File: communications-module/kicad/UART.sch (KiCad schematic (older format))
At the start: 20 parts, among them U11 FONA_3G, U12 TPS2064, U13 RockBLOCK, U14 SN74LV4052A, U15 TPS2064, U16 FGPMMOPA6H, U17 uFL_conn, U18 SN74LV4052A, U19 Gateway Module LORA

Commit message: Communications Module update
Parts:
- JP18, JP19, JP20, JP21: footprint (none) -> Socket_Strips:Socket_Strip_Straight_1x02_Pitch2.54mm
- JP22: renamed from JP?; footprint (none) -> Socket_Strips:Socket_Strip_Straight_1x02_Pitch2.54mm
- gave numbers to parts that had none: 1

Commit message: Communications Module update
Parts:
- U11: footprint FONA_3G:FONA_3G -> FONA_3G:FONA_3G_vertical
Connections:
- net FONA_3V3: no longer U20.7 (OUT1)
- net FONA_VBAT: now also U20.7 (OUT1)
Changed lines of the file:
@@
 U 1 1 589D996F
 P 1425 2045
-F 0 "U11" H 1325 3195 60  0000 C CNN
+F 0 "U11" H 1370 3190 60  0000 C CNN
 F 1 "FONA_3G" H 1475 3095 60  0000 C CNN
-F 2 "FONA_3G:FONA_3G" H 1500 1070 60  0001 C CNN
+F 2 "FONA_3G:FONA_3G_vertical" H 1500 1070 60  0001 C CNN
 F 3 "" H 1475 3170 60  0000 C CNN
 	1    1425 2045
@@
 U 1 1 589D9A2E
 P 3495 2160
-F 0 "U13" H 3520 3060 60  0000 C CNN
+F 0 "U13" H 3500 3055 60  0000 C CNN
 F 1 "RockBLOCK" H 3520 2960 60  0000 C CNN
 F 2 "" H 3545 3035 60  0000 C CNN
@@
 Wire Wire Line
 	2740 4605 2865 4605
-Text GLabel 2865 4415 2    60   Input ~ 0
-FONA_3V3
 Text GLabel 1760 4490 0    60   Input ~ 0
 ENABLE-FONA
@@
 Wire Wire Line
 	2740 4415 2865 4415
+Text GLabel 2865 4415 2    60   Input ~ 0
+FONA_VBAT
 $EndSCHEMATC

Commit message: All gerbers update
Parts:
- added R?: 10K, 0603_handsolder:0603_HandSoldering, symbol R
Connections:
- net ENABLE-ROCK: now also R?.2
- net FONA_CTS: now also U11.8 (RTS_IN); no longer U11.10 (CTS)
- net FONA_RTS: now also U11.10 (CTS); no longer U11.8 (RTS_IN)
- net FONA_RX: now also U11.7 (TX); no longer U11.6 (RX)
- net FONA_TX: now also U11.6 (RX); no longer U11.7 (TX)
- net ROCK_CTS: no longer U13.5 (CTS)
- net ROCK_RX: now also U13.3 (TXD); no longer U13.2 (RXD)
- net ROCK_TX: now also U13.2 (RXD); no longer U13.3 (TXD)
- net at U13.12 (ON_OFF): now also R?.1
- net FONA_DTR: no longer names the net of U11.9 (DTR)
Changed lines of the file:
@@
 	0    -1   -1   0
 $EndComp
+Text GLabel 1850 1745 2    60   Input ~ 0
+FONA_RX
 Text GLabel 1850 1645 2    60   Input ~ 0
-FONA_RX
-Text GLabel 1850 1745 2    60   Input ~ 0
 FONA_TX
 NoConn ~ 1850 2545
@@
 Text GLabel 4870 6220 0    60   Input ~ 0
 FONA_CTS
+Text GLabel 1850 2045 2    60   Input ~ 0
+FONA_RTS
 Text GLabel 1850 1845 2    60   Input ~ 0
-FONA_RTS
-Text GLabel 1850 2045 2    60   Input ~ 0
 FONA_CTS
 NoConn ~ 4870 5820
@@
 	1    0    0    -1
 $EndComp
+Text GLabel 3895 1585 2    60   Input ~ 0
+ROCK_TX
 Text GLabel 3895 1685 2    60   Input ~ 0
-ROCK_TX
-Text GLabel 3895 1585 2    60   Input ~ 0
 ROCK_RX
 Text GLabel 3895 1485 2    60   Input ~ 0
 ROCK_RTS
-Text GLabel 3895 1885 2    60   Input ~ 0
+Text GLabel 4540 1330 2    60   Input ~ 0
 ROCK_CTS
 $Comp
@@
 	0    -1   -1   0
 $EndComp
-Text GLabel 1850 1945 2    60   Input ~ 0
-FONA_DTR
 Text GLabel 3895 1785 2    60   Input ~ 0
 ROCK_5V
-NoConn ~ 3895 2585
 $Comp
 L +3.3V #PWR096
@@
 Text GLabel 2865 4415 2    60   Input ~ 0
 FONA_VBAT
+$Comp
+L R R?
+U 1 1 5894C116
+P 4045 2585
+F 0 "R?" V 4125 2585 50  0000 C CNN
+F 1 "10K" V 4045 2585 50  0000 C CNN
+F 2 "0603_handsolder:0603_HandSoldering" V 3975 2585 30  0001 C CNN
+F 3 "" H 4045 2585 30  0000 C CNN
+	1    4045 2585
+	0    -1   -1   0
+$EndComp
+Text GLabel 4195 2585 2    60   Input ~ 0
+ENABLE-ROCK
+NoConn ~ 1850 1945
 $EndSCHEMATC

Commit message: Communications Module schematic update
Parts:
- gave numbers to parts that had none: 1
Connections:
- net FONA_CTS: now also U14.14 (1Y1); no longer U14.5 (2Y1)
- net FONA_RTS: now also U14.5 (2Y1); no longer U14.14 (1Y1)
- net FONA_RX: now also U18.5 (2Y1); no longer U18.14 (1Y1)
- net FONA_TX: now also U18.14 (1Y1); no longer U18.5 (2Y1)
- net GPS_RX: now also U16.9 (TX), U18.1 (2Y0); no longer U16.10 (RX), U18.12 (1Y0)
- net GPS_TX: now also U16.10 (RX), U18.12 (1Y0); no longer U16.9 (TX), U18.1 (2Y0)
- net ROCK_CTS: now also U13.5 (CTS), U14.15 (1Y2); no longer U14.2 (2Y2)
- net ROCK_RTS: now also U14.2 (2Y2); no longer U14.15 (1Y2)
- net ROCK_RX: now also U13.2 (RXD), U18.2 (2Y2); no longer U13.3 (TXD), U18.15 (1Y2)
- net ROCK_TX: now also U13.3 (TXD), U18.15 (1Y2); no longer U13.2 (RXD), U18.2 (2Y2)
- net UART_A renamed UMUX_SEL0
- net UART_B renamed UMUX_SEL1
- net UART_INH renamed UMUX_INH
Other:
- moved on the sheet: JP18, JP19, JP22, U12, U14, U17, U20

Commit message: Communications Module update
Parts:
- U13: footprint (none) -> RockBlock:RockBlock_vertical
- U19: footprint RaspberryPi:RaspberryPi -> (none)
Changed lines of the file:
@@
 F 0 "U13" H 3500 3055 60  0000 C CNN
 F 1 "RockBLOCK" H 3520 2960 60  0000 C CNN
-F 2 "" H 3545 3035 60  0000 C CNN
+F 2 "RockBlock:RockBlock_vertical" H 3615 1315 60  0001 C CNN
 F 3 "" H 3545 3035 60  0000 C CNN
 	1    3495 2160
@@
 F 0 "U19" H 9445 3295 60  0000 C CNN
 F 1 "Gateway Module LORA" H 9450 3195 60  0000 C CNN
-F 2 "RaspberryPi:RaspberryPi" H 9405 1030 60  0001 C CNN
+F 2 "" H 9405 1030 60  0001 C CNN
 F 3 "" H 9405 2080 60  0000 C CNN
 	1    9405 2080

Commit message: Communications Module footprints update
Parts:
- U19: footprint (none) -> Solarcast_Gateway_Module:Solarcast_Gateway_Module
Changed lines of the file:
@@
 F 0 "U19" H 9445 3295 60  0000 C CNN
 F 1 "Gateway Module LORA" H 9450 3195 60  0000 C CNN
-F 2 "" H 9405 1030 60  0001 C CNN
+F 2 "Solarcast_Gateway_Module:Solarcast_Gateway_Module" H 9405 1030 60  0001 C CNN
 F 3 "" H 9405 2080 60  0000 C CNN
 	1    9405 2080

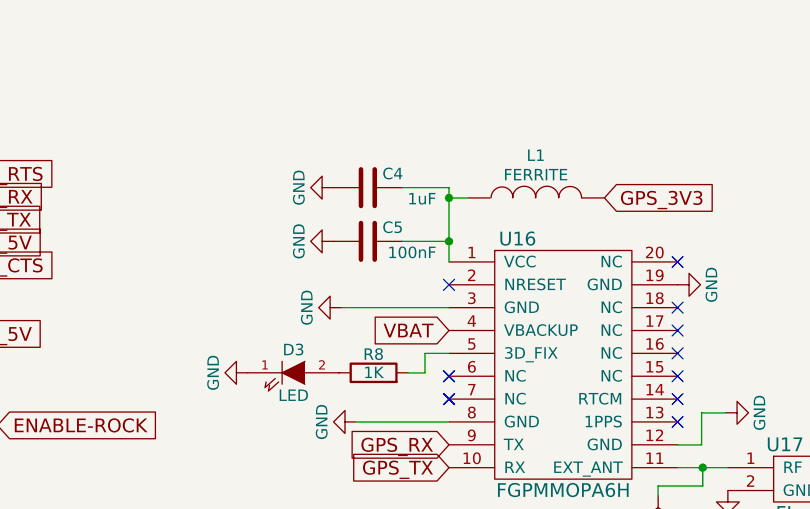
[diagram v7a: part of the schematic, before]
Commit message: Communications Module PCB components placed
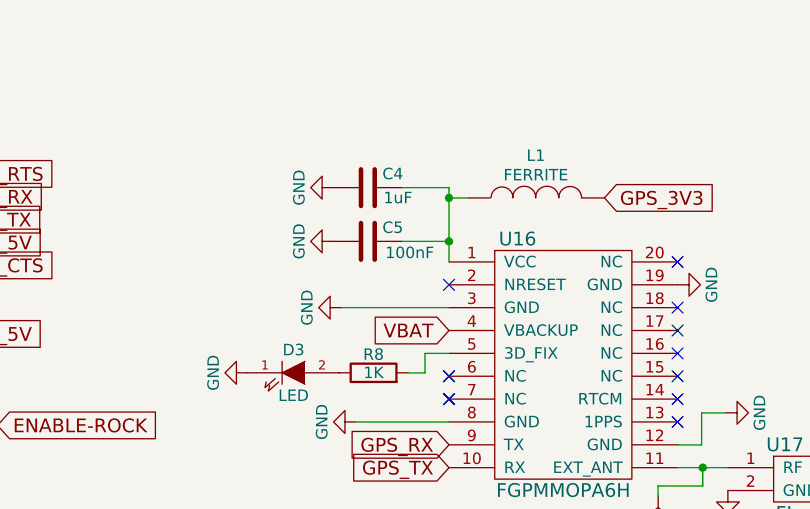
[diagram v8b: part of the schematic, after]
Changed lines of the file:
@@
 P 5815 1780
 F 0 "C5" V 5875 1625 50  0000 L CNN
-F 1 "100nF" V 5765 1480 50  0000 L CNN
+F 1 "100nF" V 5765 1490 50  0000 L CNN
 F 2 "0603_handsolder:0603_HandSoldering" H 5853 1630 30  0001 C CNN
 F 3 "" H 5815 1780 60  0000 C CNN
@@
 P 5815 1545
 F 0 "C4" V 5875 1390 50  0000 L CNN
-F 1 "1uF" V 5765 1245 50  0000 L CNN
+F 1 "1uF" V 5770 1350 50  0000 L CNN
 F 2 "0603_handsolder:0603_HandSoldering" H 5853 1395 30  0001 C CNN
 F 3 "" H 5815 1545 60  0000 C CNN
